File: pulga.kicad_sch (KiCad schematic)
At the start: 32 parts, among them J1 Conn_01x04_Pin, J2 Conn_01x04_Pin, SW1 SW_Push, SW2 SW_Push, U2 ESP32-C3-WROOM-02, U3 TCAN332G, U4 AMS1117-3.3

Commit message: corrigindo o LCSC do TPS54331
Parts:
- U1: LCSC C544741 -> C9865
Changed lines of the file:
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@@
 			)
 		)
-		(property "LCSC" "C544741"
+		(property "LCSC" "C9865"
 			(at 83.82 41.91 0)
 			(effects

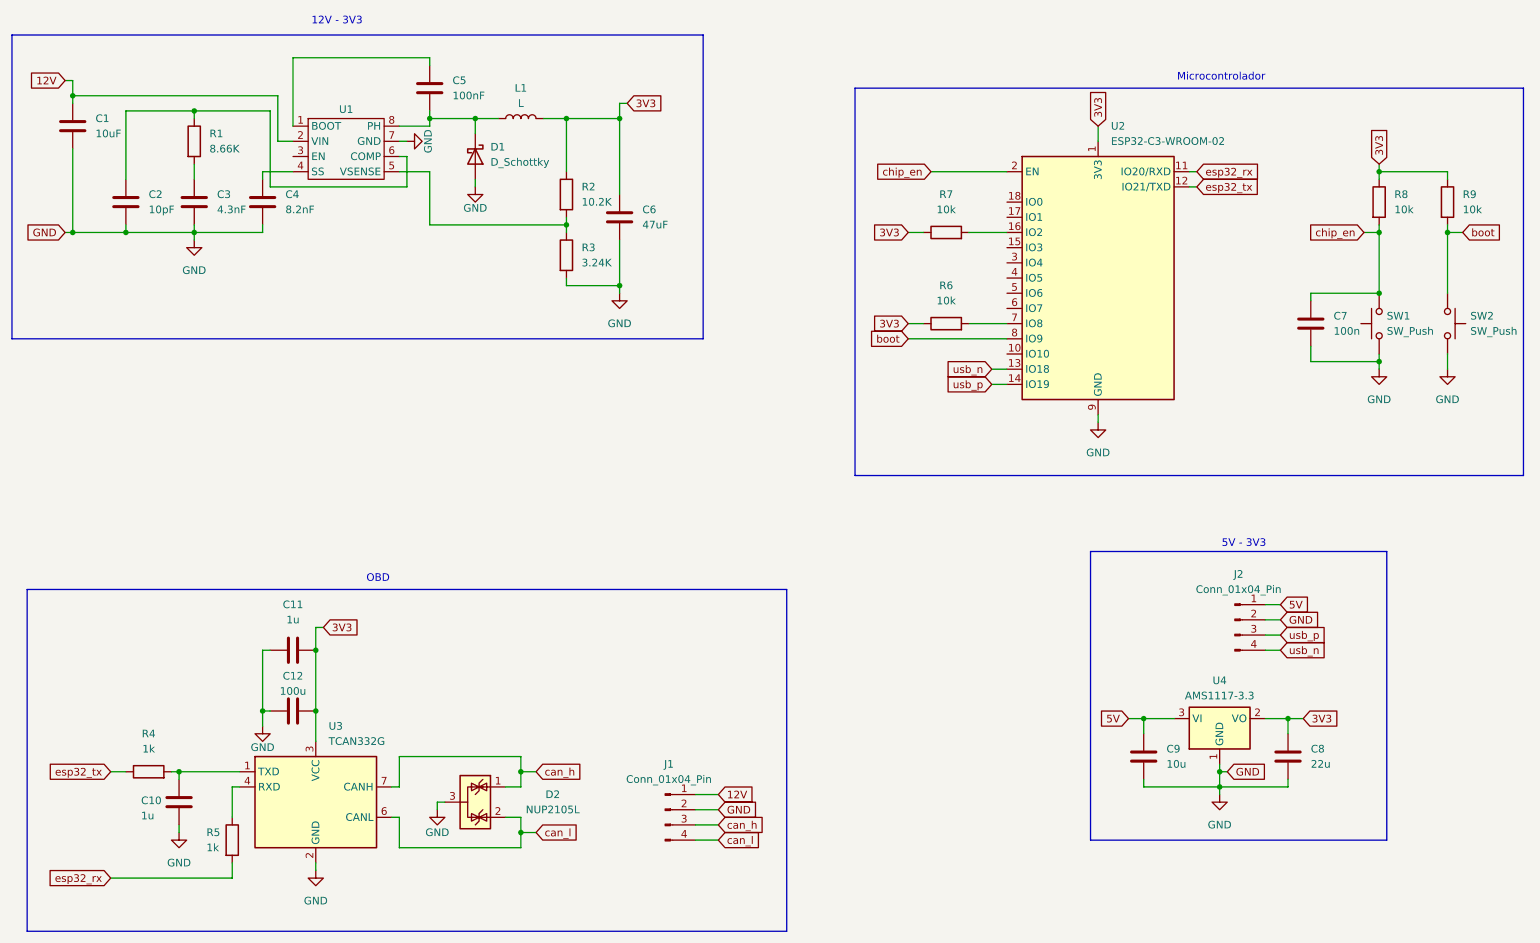
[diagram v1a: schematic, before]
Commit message: invertendo a posição do circuito can e ldo; trocando 2 conectores de 4 vias por 4 de 2 vias
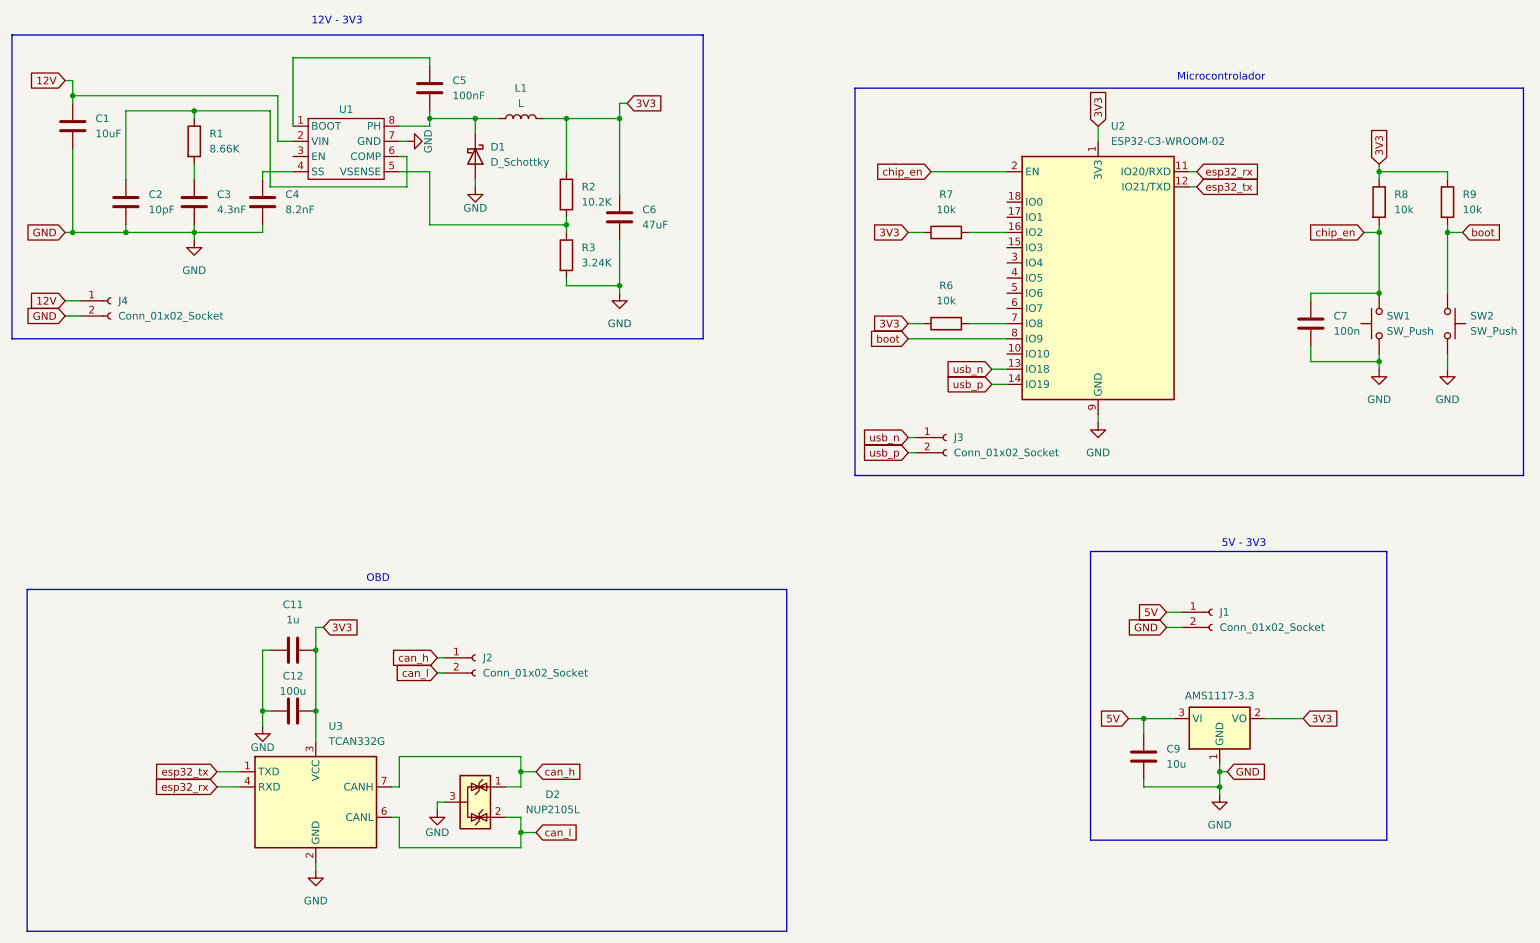
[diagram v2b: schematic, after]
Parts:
- removed C10: 1u, Capacitor_SMD:C_0201_0603Metric, symbol Device:C
- removed C8: 22u, Capacitor_SMD:C_1206_3216Metric, symbol Device:C
- removed J1, J2: Conn_01x04_Pin, through_hole:obd_main_pins, symbol Connector:Conn_01x04_Pin
- removed R4, R5: 1k, Resistor_SMD:R_0402_1005Metric, symbol Device:R
- added J1, J2, J3, J4: Conn_01x02_Socket, through_hole:two_th_pins, symbol Connector:Conn_01x02_Socket
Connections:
- net 12V: now also J4.1 (Pin_1)
- net 5V: now also J1.1 (Pin_1)
- net GND: now also J1.2 (Pin_2), J4.2 (Pin_2)
- net can_h: now also J2.1 (Pin_1)
- net can_l: now also J2.2 (Pin_2)
- net esp32_rx: now also U3.4 (RXD)
- net esp32_tx: now also U3.1 (TXD)
- net usb_n: now also J3.1 (Pin_1)
- net usb_p: now also J3.2 (Pin_2)
